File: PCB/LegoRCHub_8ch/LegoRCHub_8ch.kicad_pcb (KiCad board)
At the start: 2 copper layers, 39.3 x 55.2 mm, 38 parts, among them J1 Conn_01x02, J10 Conn_01x02, J11 Conn_01x03, J2 Conn_01x02, J3 Conn_01x02, J4 Conn_01x02, J5 Conn_01x02, J6 Conn_01x03, J7 Conn_01x03, J8 Conn_01x03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

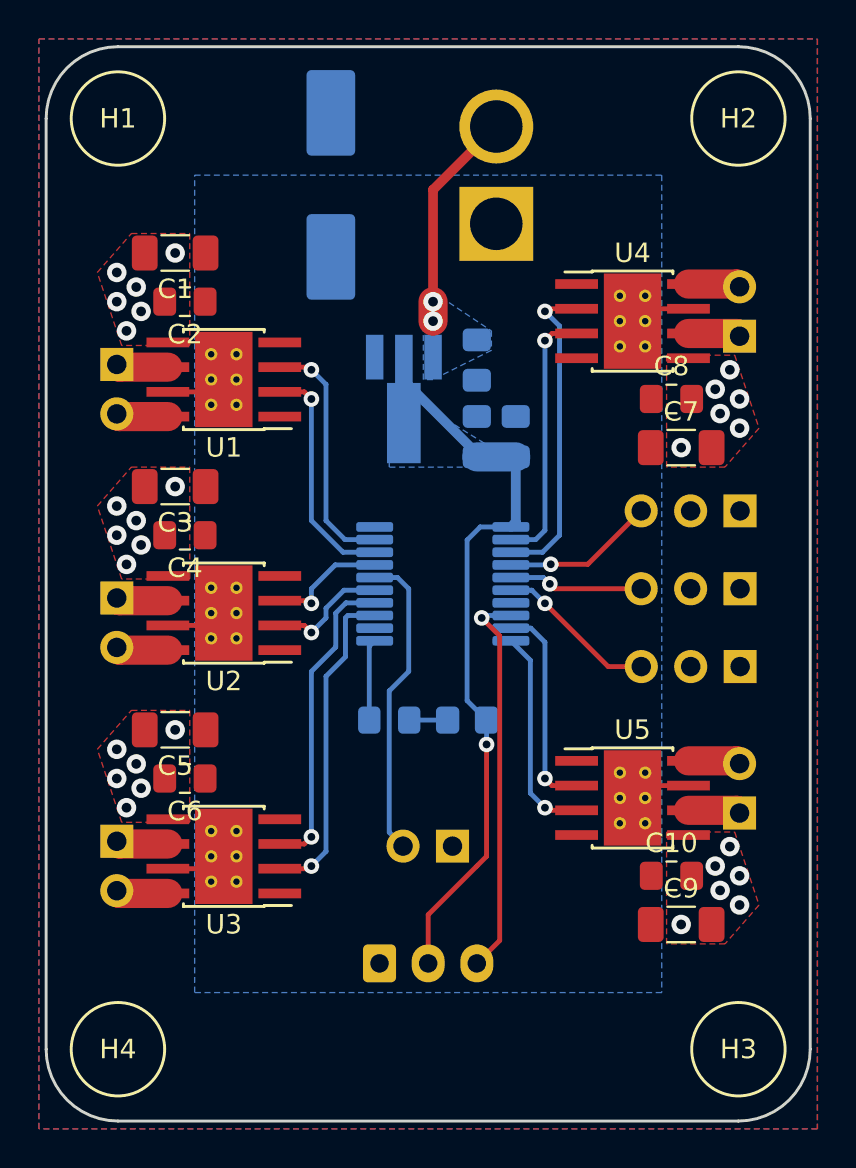
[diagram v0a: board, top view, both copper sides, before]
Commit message: LegoRCHub_8ch: beta 6: simplified design with 4/4 layout
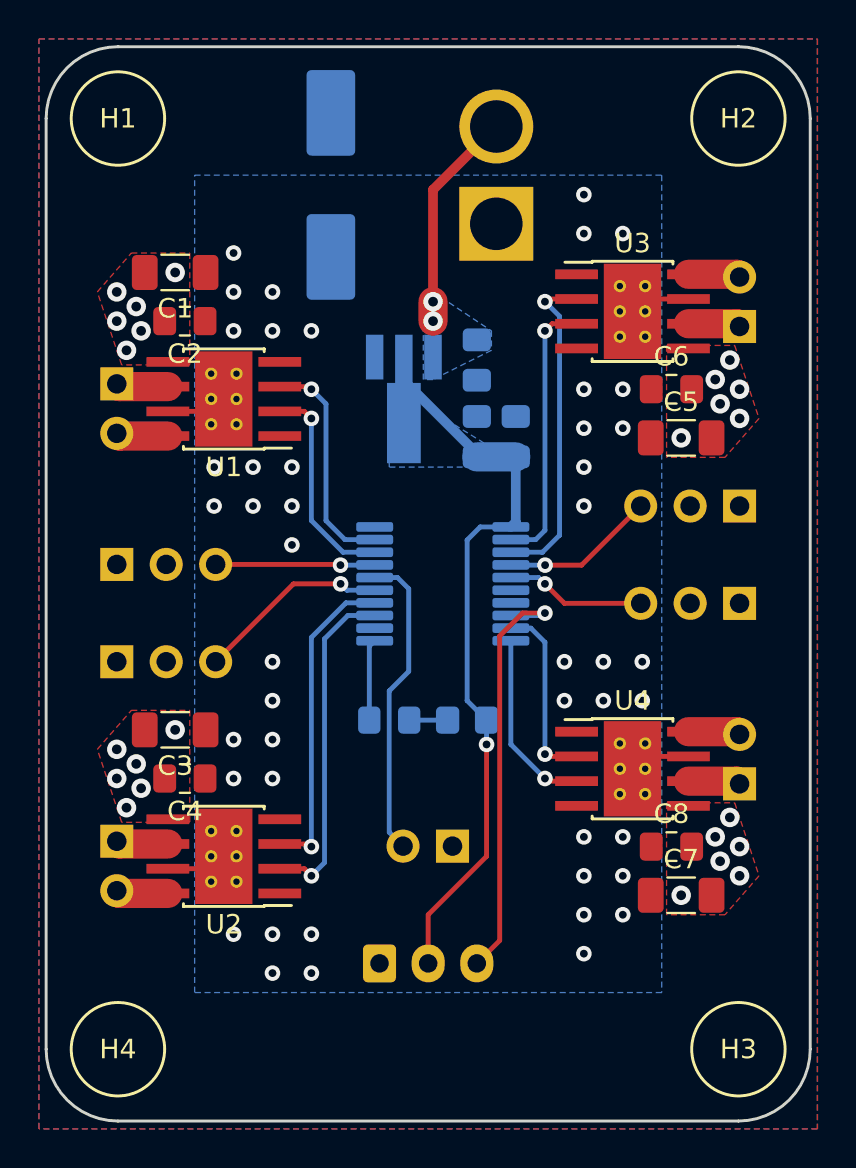
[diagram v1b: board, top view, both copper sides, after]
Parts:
- removed C10: 100nF, Capacitor_SMD:C_0805_2012Metric_Pad1.18x1.45mm_HandSolder
- removed C9: 47uF, Capacitor_SMD:C_1206_3216Metric_Pad1.33x1.80mm_HandSolder
- removed U5: DRV8872DDA, Package_SO:Texas_HTSOP-8-1EP_3.9x4.9mm_P1.27mm_EP2.95x4.9mm_Mask2.4x3.1mm_ThermalVias
- J5: value Conn_01x02 -> Conn_01x03; footprint Connector_PinHeader_2.54mm:PinHeader_1x02_P2.54mm_Vertical -> Connector_PinHeader_2.54mm:PinHeader_1x03_P2.54mm_Vertical
- moved J3 41.5 mm to (60.5, 37.6), turned to 0 degrees
- moved U3 35.0 mm to (55.0, 36.8), turned to 0 degrees
- moved J5 34.5 mm to (28.4, 49.8), turned to -90 degrees
- moved J6 32.9 mm to (28.4, 54.8), turned to -90 degrees
- moved C6 32.0 mm to (57.0, 40.8), turned to 0 degrees
- moved C5 30.0 mm to (57.5, 43.3), turned to 0 degrees
- moved C7 23.0 mm to (57.5, 66.8)
- moved C8 23.0 mm to (57.0, 64.3)
- moved J4 23.0 mm to (60.5, 61.1)
- moved U4 23.0 mm to (55.0, 60.3)
- moved J2 12.5 mm to (28.4, 64.0)
- moved C3 12.5 mm to (31.4, 58.3)
- moved U2 12.5 mm to (34.0, 64.8)
- moved C4 12.5 mm to (31.9, 60.8)
- moved J7 4.25 mm to (60.5, 46.8)
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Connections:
- J5 pad 1: Net-(J5-Pad1) -> GND
- J5 pad 2: Net-(J5-Pad2) -> +BATT
- U7 pad 10: /CH5_3 -> /CH4_3
- U7 pad 13: /CH3_2 -> /CH2_2
- U7 pad 14: /CH3_3 -> /CH2_3
- U7 pad 15: /CH2_2 -> /CH6
- U7 pad 17: /CH2_3 -> /CH5
- U7 pad 2: /CH4_3 -> /CH3_3
- U7 pad 3: /CH4_2 -> /CH3_2
- U7 pad 4: /CH6 -> /CH7
- U7 pad 5: /CH7 -> /CH8
- U7 pad 6: /CH8 -> unconnected-(U7-Pad6)
- U7 pad 9: /CH5_2 -> /CH4_2
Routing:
- net /CH2_2: track 6.22 -> 17.3 mm
- net /CH5_3: track 11.0 -> 0.00 mm, vias 1 -> 0
- net /CH5_2: track 10.8 -> 0.00 mm, vias 1 -> 0
- net /CH2_3: track 6.19 -> 16.4 mm
- net /CH5: track 0.00 -> 8.17 mm, vias 0 -> 1
- net /CH4_2: track 16.4 -> 9.47 mm
- net /CH4_3: track 13.5 -> 9.48 mm
- net Net-(J5-Pad2): track 2.68 -> 0.00 mm
- net Net-(J5-Pad1): track 2.68 -> 0.00 mm
- net /CH6: track 7.84 -> 9.96 mm
- net /CH3_3: track 16.0 -> 14.0 mm
- net /IBus: track 20.2 -> 21.9 mm
- net GND: track 7.95 -> 6.36 mm, vias 0 -> 45
- net VCC: track 38.1 -> 36.9 mm
- net /CH8: track 8.33 -> 7.22 mm
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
